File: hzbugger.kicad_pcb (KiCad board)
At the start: 2 copper layers, 53.5 x 26.7 mm, 56 parts, among them J2 IDC, J4 SWD, J6 GPIO, SW1 RESET_SW, SW2 BOOT0_SW, U1 STM32F103C8T6, U2 SRV05-4, U3 AMS1117-3.3, U4 HX AM 90D, Y1 8M

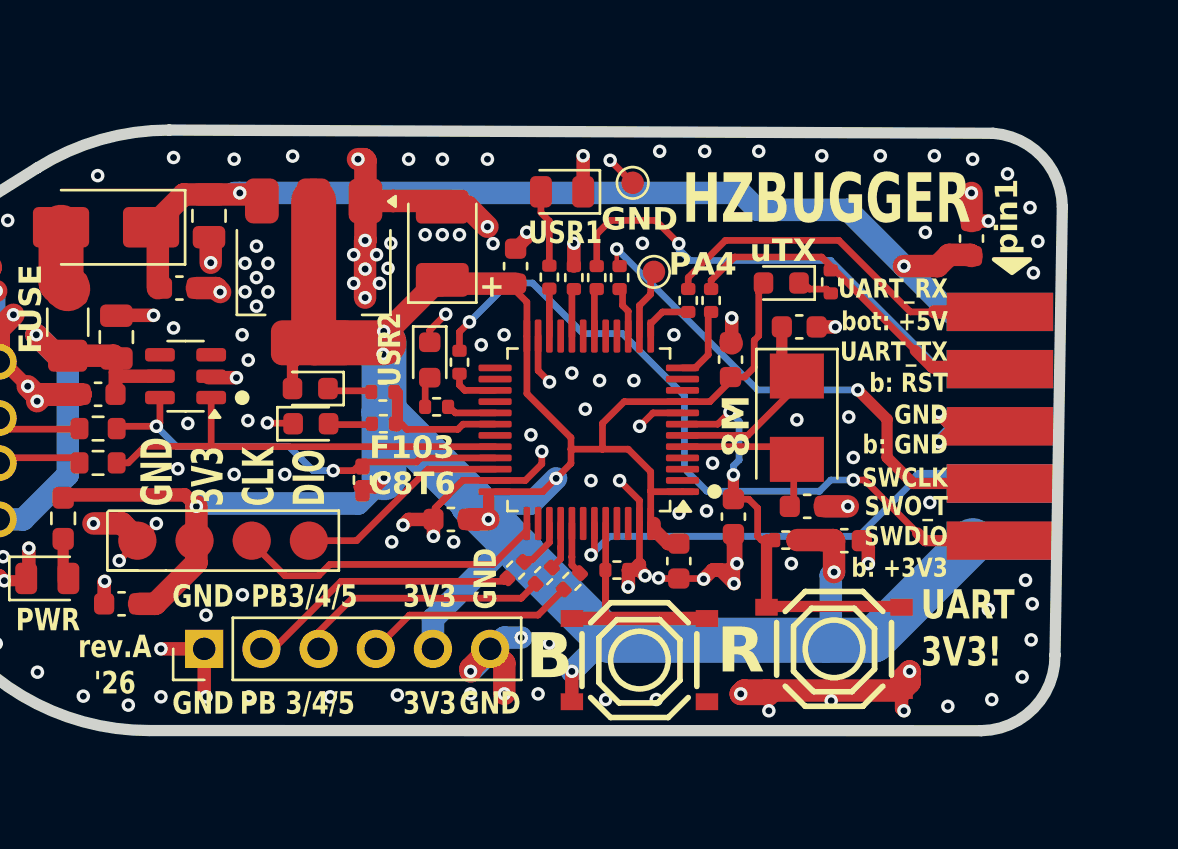
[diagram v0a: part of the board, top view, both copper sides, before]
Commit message: hole for keychain
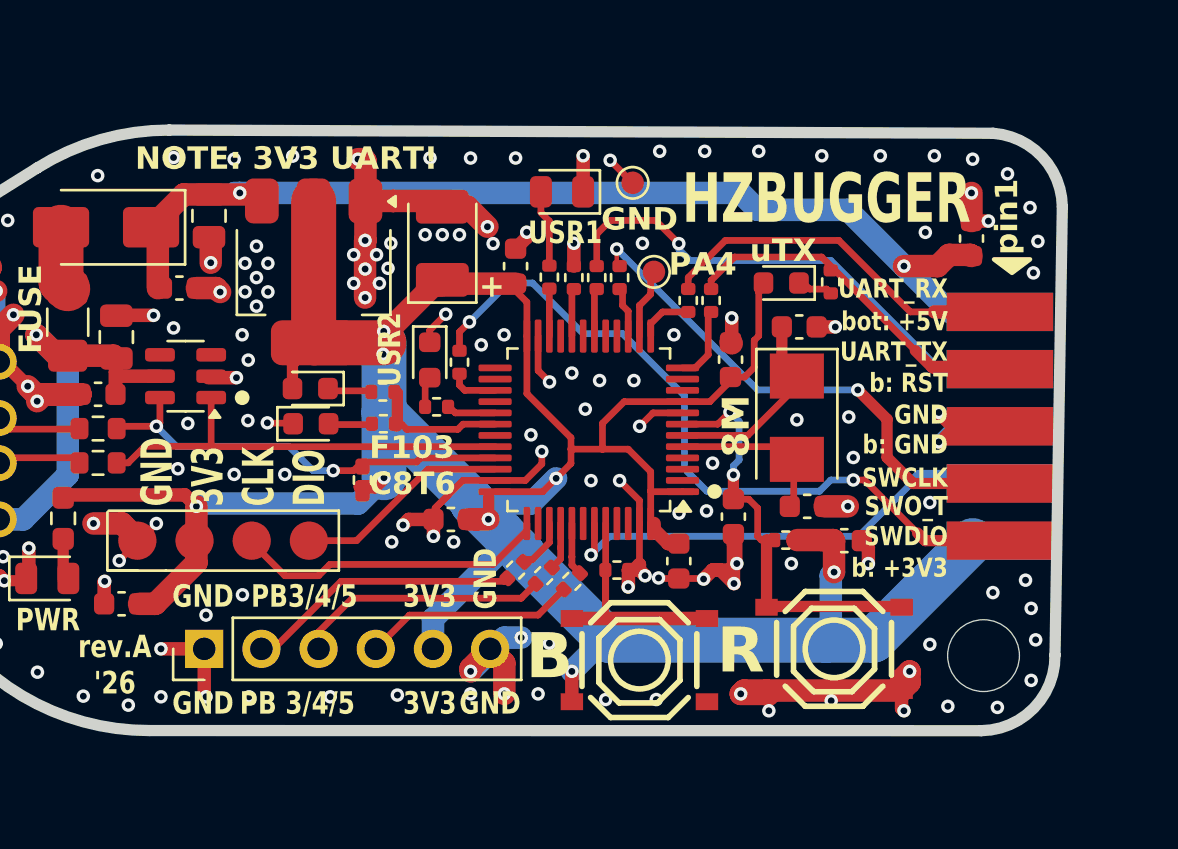
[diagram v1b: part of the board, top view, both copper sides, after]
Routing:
- net GND: vias 163 -> 164
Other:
- outline, holes or cut-outs redrawn
- board text added: "NOTE: 3V3 UART!"
- board text removed: "UART 3V3!"
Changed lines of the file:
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@@
 		(layer "Edge.Cuts")
 	)
+	(gr_circle
+		(center 150.78391 96.8)
+		(end 152.1 97.7)
+		(stroke
+			(width 0.05)
+			(type solid)
+		)
+		(fill no)
+		(layer "Edge.Cuts")
+	)
 	(gr_line
 		(start 153.958794 96.777598)
@@
 		)
 	)
-	(gr_text "UART\n3V3!"
-		(at 148 97.4 0)
-		(layer "F.SilkS" knockout)
+	(gr_text "NOTE: 3V3 UART!"
+		(at 113.1 75.3 0)
+		(layer "F.SilkS")
 		(effects
 			(font
-				(size 1.3 1)
+				(size 1 1)
 				(thickness 0.25)
 				(bold yes)
@@
 	)
 	(via
-		(at 128.75 74.75)
+		(at 130 74.7)
 		(size 0.6)
 		(drill 0.3)
@@
 	)
 	(via
-		(at 152.9 96.1)
+		(at 153.1 96.1)
 		(size 0.6)
 		(drill 0.3)
@@
 	)
 	(via
+		(at 148.4 96.3)
+		(size 0.6)
+		(drill 0.3)
+		(layers "F.Cu" "B.Cu")
+		(free yes)
+		(net 9)
+	)
+	(via
 		(at 138.4808 90.3732)
 		(size 0.6)
@@
 	)
 	(via
-		(at 151.15 98.75)
+		(at 151.4 99.1)
 		(size 0.6)
 		(drill 0.3)
@@
 	)
 	(via
-		(at 126.75 74.75)
+		(at 128 74.7)
 		(size 0.6)
 		(drill 0.3)
@@
 	)
 	(via
-		(at 152.95 94.5)
+		(at 152.9 94.7)
 		(size 0.6)
 		(drill 0.3)
@@
 	)
 	(via
-		(at 152.5 97.75)
+		(at 152.9 97.9)
 		(size 0.6)
 		(drill 0.3)
@@
 	)
 	(via
-		(at 151 94.75)
+		(at 151.2 94)
 		(size 0.6)
 		(drill 0.3)
@@
 	)
 	(via
-		(at 125.25 74.75)
+		(at 126.2 74.7)
 		(size 0.6)
 		(drill 0.3)

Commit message: drc
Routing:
- net GND: vias 164 -> 163
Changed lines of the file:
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@@
 	)
 	(via
-		(at 153.1 96.1)
+		(at 153.1 95.5)
 		(size 0.6)
 		(drill 0.3)
@@
 	)
 	(via
-		(at 151.4 99.1)
-		(size 0.6)
-		(drill 0.3)
-		(layers "F.Cu" "B.Cu")
-		(free yes)
-		(net 9)
-	)
-	(via
 		(at 152.85 76.9)
 		(size 0.6)
@@
 	)
 	(via
+		(at 148.6 98.4)
+		(size 0.6)
+		(drill 0.3)
+		(layers "F.Cu" "B.Cu")
+		(free yes)
+		(net 9)
+	)
+	(via
 		(at 117.983 80.645)
 		(size 0.6)
@@
 		(net 9)
 	)
-	(via
-		(at 152.9 97.9)
-		(size 0.6)
-		(drill 0.3)
-		(layers "F.Cu" "B.Cu")
-		(free yes)
-		(net 9)
-	)

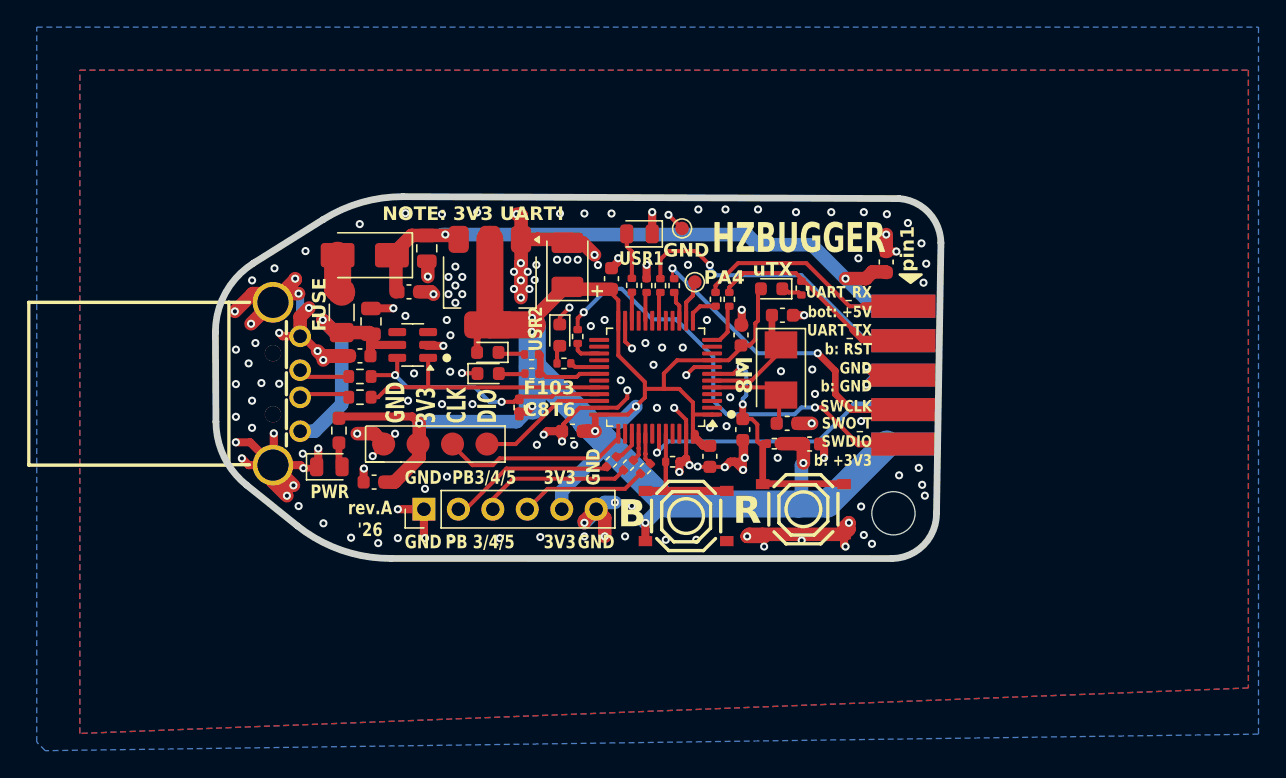
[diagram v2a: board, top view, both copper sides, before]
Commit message: some enhancements, corrected LCSC code for 0422 1k5 R
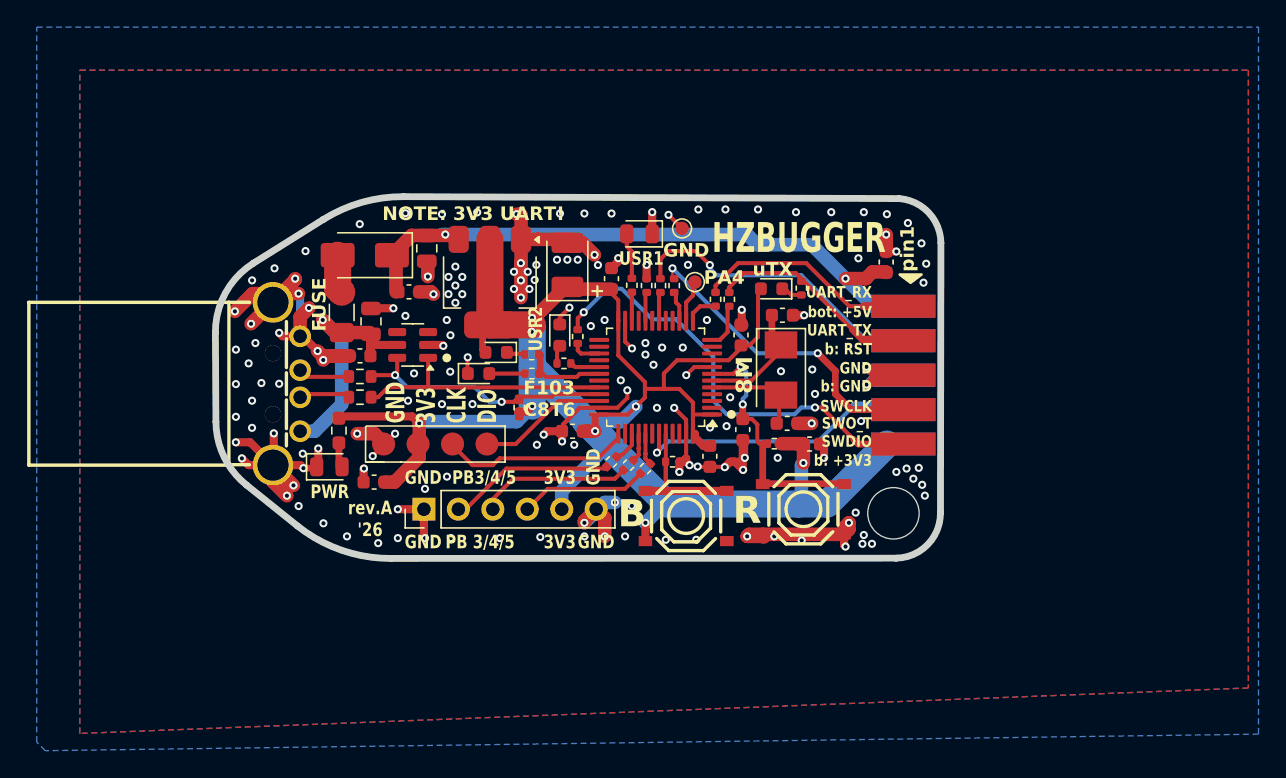
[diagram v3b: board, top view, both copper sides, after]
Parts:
- moved D3 0.71 mm to (120.2, 86.5)
- moved D4 0.62 mm to (121.5, 84.9)
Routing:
- net Net-(D3-A): track 1.96 -> 2.63 mm
- net Net-(D4-K): track 1.95 -> 1.37 mm
- net GND: vias 163 -> 167
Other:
- outline, holes or cut-outs redrawn

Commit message: fine-tuning
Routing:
- net VBUS: track 20.0 -> 20.5 mm
- net GND: vias 167 -> 168
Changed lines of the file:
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@@
 	)
 	(segment
-		(start 121.0056 88.583)
-		(end 119.9256 87.503)
+		(start 121.6693 88.583)
+		(end 120.5893 87.503)
 		(width 0.3)
 		(layer "B.Cu")
@@
 	)
 	(segment
-		(start 114.935 87.503)
-		(end 114.046 86.614)
+		(start 120.5893 87.503)
+		(end 114.935 87.503)
 		(width 0.3)
 		(layer "B.Cu")
@@
 	)
 	(segment
-		(start 119.9256 87.503)
-		(end 114.935 87.503)
+		(start 121.9 88.583)
+		(end 121.6693 88.583)
 		(width 0.3)
 		(layer "B.Cu")
@@
 	)
 	(segment
-		(start 121.9 88.583)
-		(end 121.0056 88.583)
+		(start 114.935 87.503)
+		(end 114.046 86.614)
 		(width 0.3)
 		(layer "B.Cu")
@@
 	)
 	(segment
-		(start 144 93.236)
+		(start 144.25 93.196)
 		(end 144.145 93.091)
 		(width 1)
@@
 	)
 	(segment
+		(start 144.25 95.653)
+		(end 144.25 93.196)
+		(width 1)
+		(layer "B.Cu")
+		(net 4)
+	)
+	(segment
 		(start 115.951 90.043)
 		(end 115.824 90.17)
@@
 	)
 	(segment
-		(start 143.7894 96.1136)
-		(end 144 95.903)
-		(width 1)
+		(start 145.8864 96.1136)
+		(end 150.306 91.694)
+		(width 2)
 		(layer "B.Cu")
 		(net 4)
 	)
 	(segment
-		(start 144 95.903)
-		(end 144 93.236)
+		(start 143.7894 96.1136)
+		(end 144.25 95.653)
 		(width 1)
 		(layer "B.Cu")
@@
 	)
 	(segment
-		(start 145.8864 96.1136)
-		(end 150.306 91.694)
-		(width 2)
-		(layer "B.Cu")
-		(net 4)
-	)
-	(segment
 		(start 130.302 92.2528)
 		(end 130.302 92.302)
@@
 	)
 	(via
+		(at 108.5 89)
+		(size 0.6)
+		(drill 0.3)
+		(layers "F.Cu" "B.Cu")
+		(free yes)
+		(net 9)
+	)
+	(via
 		(at 120.09824 74.615345)
 		(size 0.6)
@@
 	)
 	(segment
-		(start 110.109 83.947)
-		(end 110.109 88.773)
+		(start 110.109 89.641)
+		(end 109.001 90.749)
 		(width 1)
 		(layer "B.Cu")
@@
 	)
 	(segment
-		(start 108.133 90.749)
-		(end 107.045 90.749)
+		(start 110.109 83.947)
+		(end 110.109 89.641)
 		(width 1)
 		(layer "B.Cu")
@@
 	)
 	(segment
-		(start 108.712 82.55)
-		(end 110.109 83.947)
+		(start 109.001 90.749)
+		(end 107.045 90.749)
 		(width 1)
 		(layer "B.Cu")
@@
 	)
 	(segment
-		(start 110.109 88.773)
-		(end 108.133 90.749)
+		(start 108.712 82.55)
+		(end 110.109 83.947)
 		(width 1)
 		(layer "B.Cu")
